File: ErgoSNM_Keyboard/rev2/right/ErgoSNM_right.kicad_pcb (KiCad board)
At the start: 2 copper layers, 115.6 x 106.7 mm, 107 parts, among them J1 USB_C_Receptacle_USB2.0, J2 USB_C_Receptacle_USB2.0, J3 PJ-393_TRRS_8P, J4 Conn_01x08, SW1 BOOT, SW2 RESET, U1 RT9013-33GB, U2 SRV05-4, U3 W25Q128JVS, U4 RP2040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

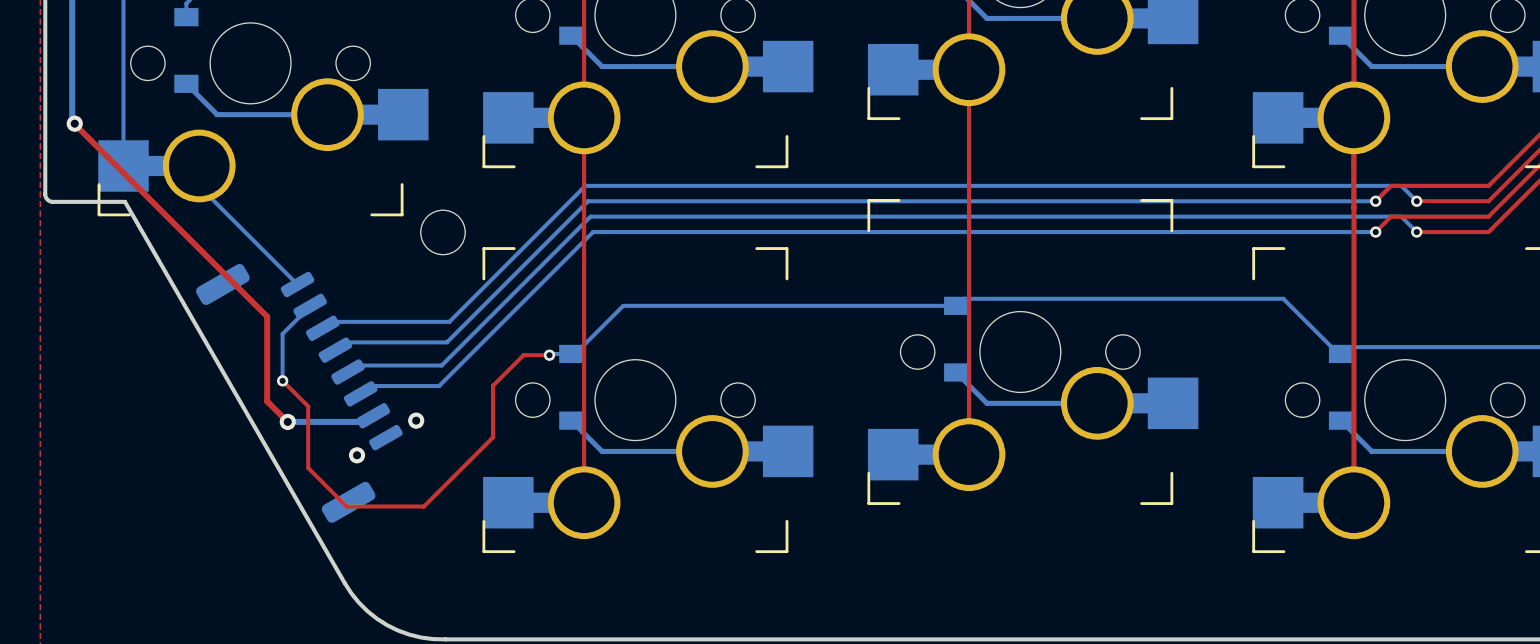
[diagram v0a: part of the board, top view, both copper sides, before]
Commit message: Replace JST GH 1.25 connector with 0.5mm FPC
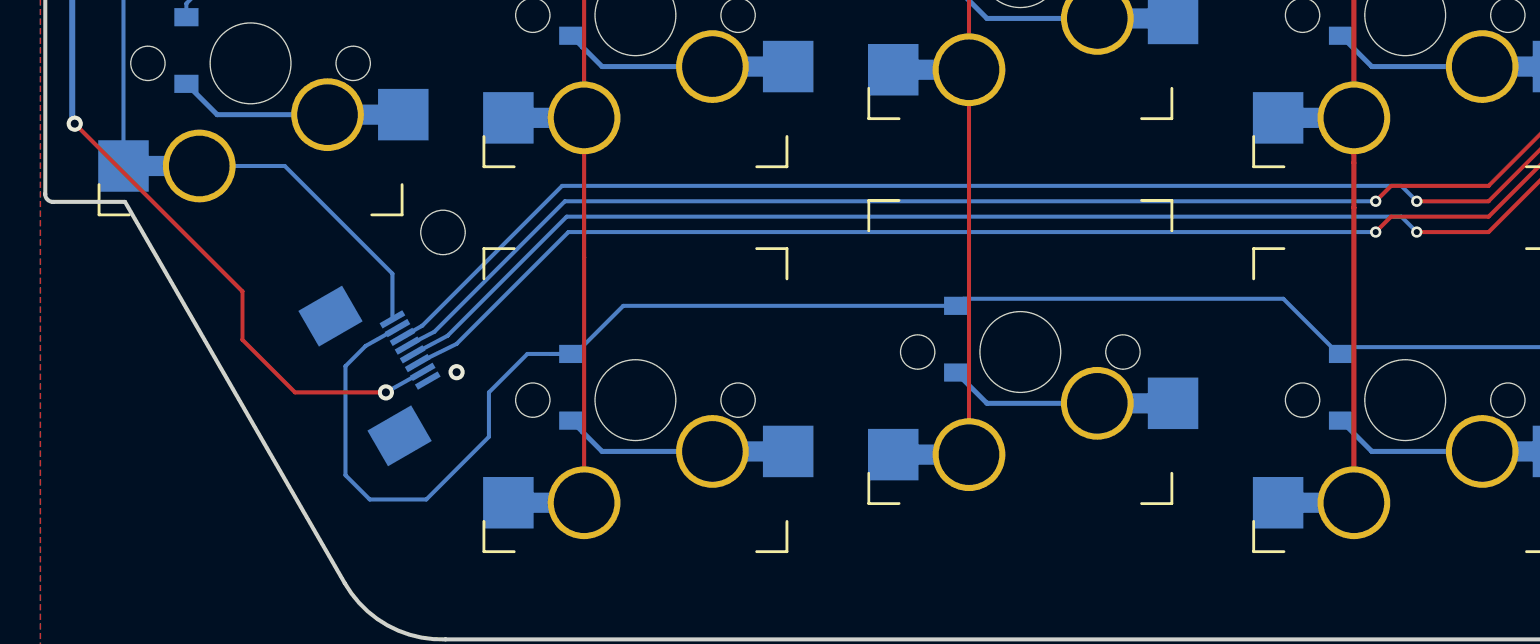
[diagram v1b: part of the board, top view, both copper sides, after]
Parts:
- removed kibuzzard-63A148C1: G***, kibuzzard-63A148C1
- J4: footprint Connector_JST:JST_GH_SM08B-GHS-TB_1x08-1MP_P1.25mm_Horizontal -> ErgoSNM_Keyboard:FPC_8P_0.5mm_AFC01-S08FCA-00
- moved J4 2.39 mm to (90.1, 124.4), turned to -60 degrees
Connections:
- J4 pad 1: GND -> COL_5
- J4 pad 2: +3V3 -> ROW_4
- J4 pad 3: ~{CS} -> SCLK
- J4 pad 4: MISO -> MOSI
- J4 pad 5: MOSI -> MISO
- J4 pad 6: SCLK -> ~{CS}
- J4 pad 7: ROW_4 -> +3V3
- J4 pad 8: COL_5 -> GND
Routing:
- net COL_5: track 173.3 -> 180.4 mm
- net SCLK: track 135.4 -> 131.5 mm
- net MOSI: track 133.7 -> 129.9 mm
- net MISO: track 145.8 -> 142.0 mm
- net ~{CS}: track 146.0 -> 142.3 mm
- net ROW_4: track 231.9 -> 229.9 mm, vias 4 -> 2
- net +3V3: track 244.0 -> 244.9 mm
- net GND: vias 59 -> 58
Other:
- board text added: "Rev ${REVISION}"

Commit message: Update FPC connection and add additional LED LD2
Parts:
- added J5: Conn_01x02, Connector_PinHeader_2.54mm:PinHeader_1x02_P2.54mm_Vertical, B.Cu at (92.1, 131.0)
- added JP1: SolderJumper_2_Open, Jumper:SolderJumper-2_P1.3mm_Open_TrianglePad1.0x1.5mm, B.Cu at (82.8, 118.8)
- added JP2: SolderJumper_2_Open, Jumper:SolderJumper-2_P1.3mm_Open_TrianglePad1.0x1.5mm, B.Cu at (85.4, 118.8)
- added LD2: LED, LED_SMD:LED_0805_2012Metric_Pad1.15x1.40mm_HandSolder, F.Cu at (180.0, 45.6)
- moved LD1 19.7 mm to (185.3, 65.8)
- moved R3 17.3 mm to (185.4, 63.6), turned to 180 degrees
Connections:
- J4 pad 1: COL_5 -> Net-(J4-Pad1)
- J4 pad 2: ROW_4 -> Net-(J4-Pad2)
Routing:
- net Net-(LD1-Pad1): track 1.61 -> 25.0 mm, vias 0 -> 1
- net STATE_LED: track 26.0 -> 47.4 mm, vias 0 -> 1
- net COL_5: track 180.4 -> 195.8 mm
- net Net-(J4-Pad2): track 0.00 -> 12.0 mm
- net Net-(J4-Pad1): track 0.00 -> 8.25 mm
- net ROW_4: track 229.9 -> 234.4 mm, vias 2 -> 3
- net GND: track 46.6 -> 45.6 mm

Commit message: Update plate
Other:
- board text added: "JLCJLCJLCJLC"
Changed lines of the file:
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@@
     (fp_line (start -1 -0.3) (end -1 0.6) (layer "F.Fab") (width 0.1))
     (fp_line (start -1 0.6) (end 1 0.6) (layer "F.Fab") (width 0.1))
-    (pad "1" smd roundrect (at -1.025 0 180) (size 1.15 1.4) (layers "F.Cu" "F.Paste" "F.Mask") (roundrect_rratio 0.217391)
+    (pad "1" smd roundrect (at -1.025 0 180) (size 1.15 1.4) (layers "F.Cu" "F.Paste" "F.Mask") (roundrect_rratio 0.2173913043)
       (net 83 "Net-(LD1-Pad1)") (pinfunction "K") (pintype "passive"))
-    (pad "2" smd roundrect (at 1.025 0 180) (size 1.15 1.4) (layers "F.Cu" "F.Paste" "F.Mask") (roundrect_rratio 0.217391)
+    (pad "2" smd roundrect (at 1.025 0 180) (size 1.15 1.4) (layers "F.Cu" "F.Paste" "F.Mask") (roundrect_rratio 0.2173913043)
       (net 84 "STATE_LED") (pinfunction "A") (pintype "passive"))
     (model "${KICAD6_3DMODEL_DIR}/LED_SMD.3dshapes/LED_0805_2012Metric.wrl"
@@
     (effects (font (size 1.2 1.2) (thickness 0.2)))
   )
+  (gr_text "JLCJLCJLCJLC" (at 184.3532 139.0396) (layer "F.SilkS")
+    (effects (font (size 1 1) (thickness 0.15)))
+  )
   (gr_text "Rev ${REVISION}" (at 169.3712 105.8296) (layer "B.Mask")
